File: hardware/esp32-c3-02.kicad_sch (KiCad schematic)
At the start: 15 parts, among them J3 GSD090012SEU, U3 ESP32-C3-WROOM-02-H4, U4 CP2102N-Axx-xQFN20, U5 USBLC6-2SC6, U6 W25Q32JVSSIQ

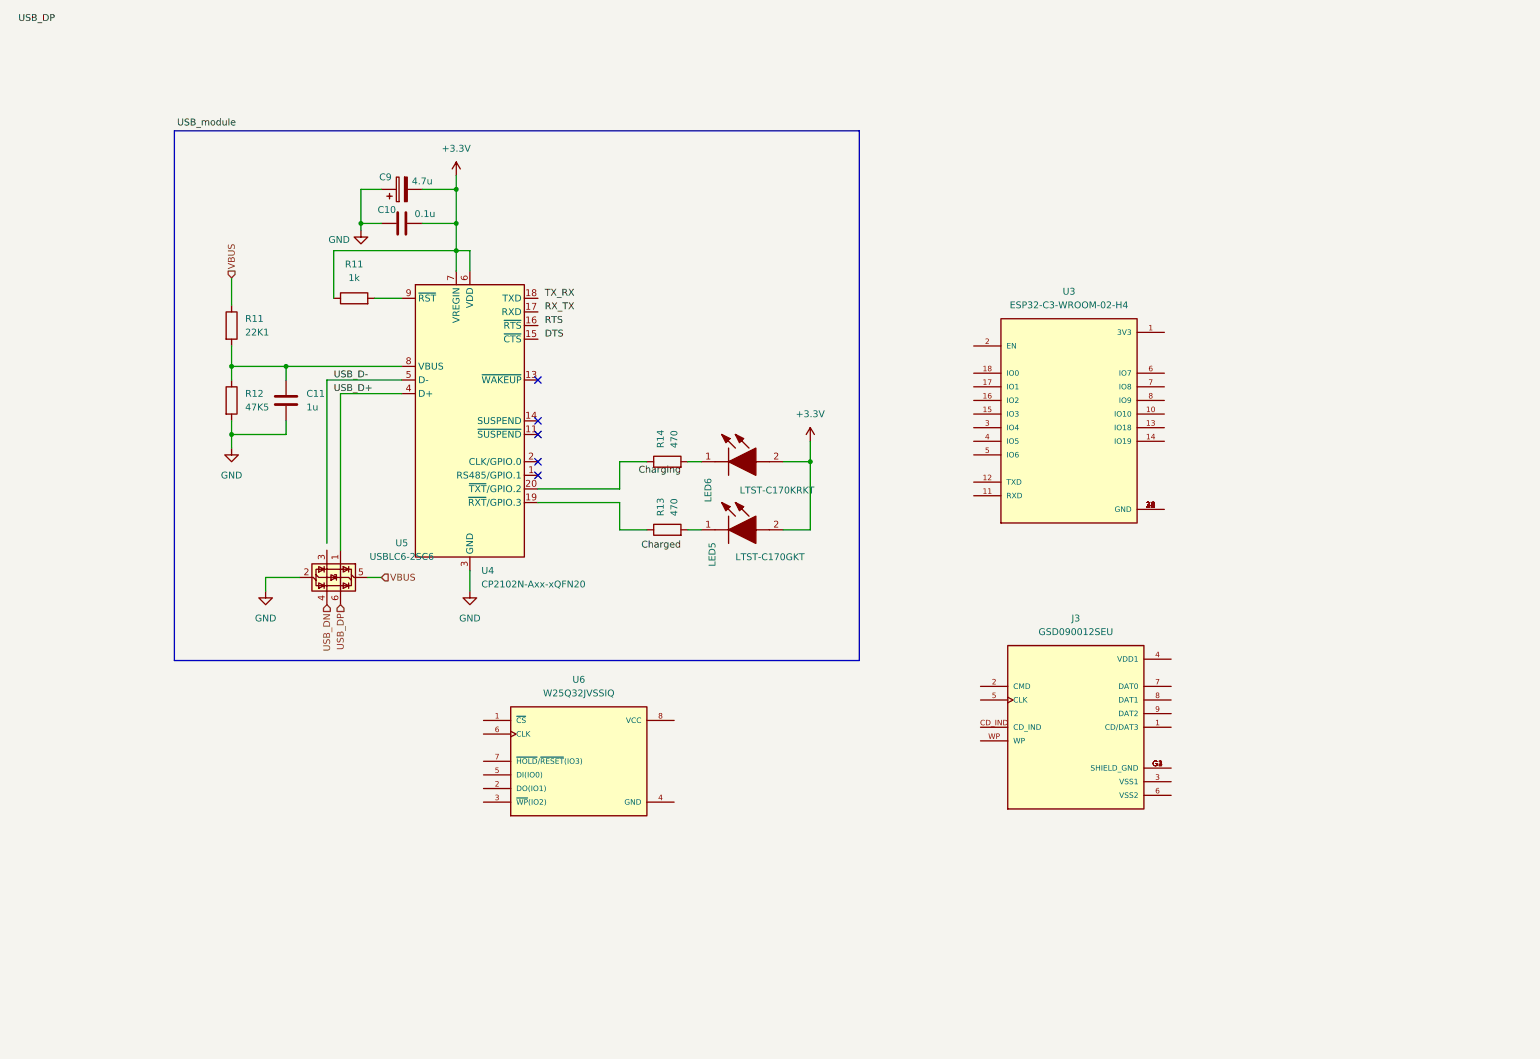
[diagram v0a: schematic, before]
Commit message: Completed the Esp32 schematics
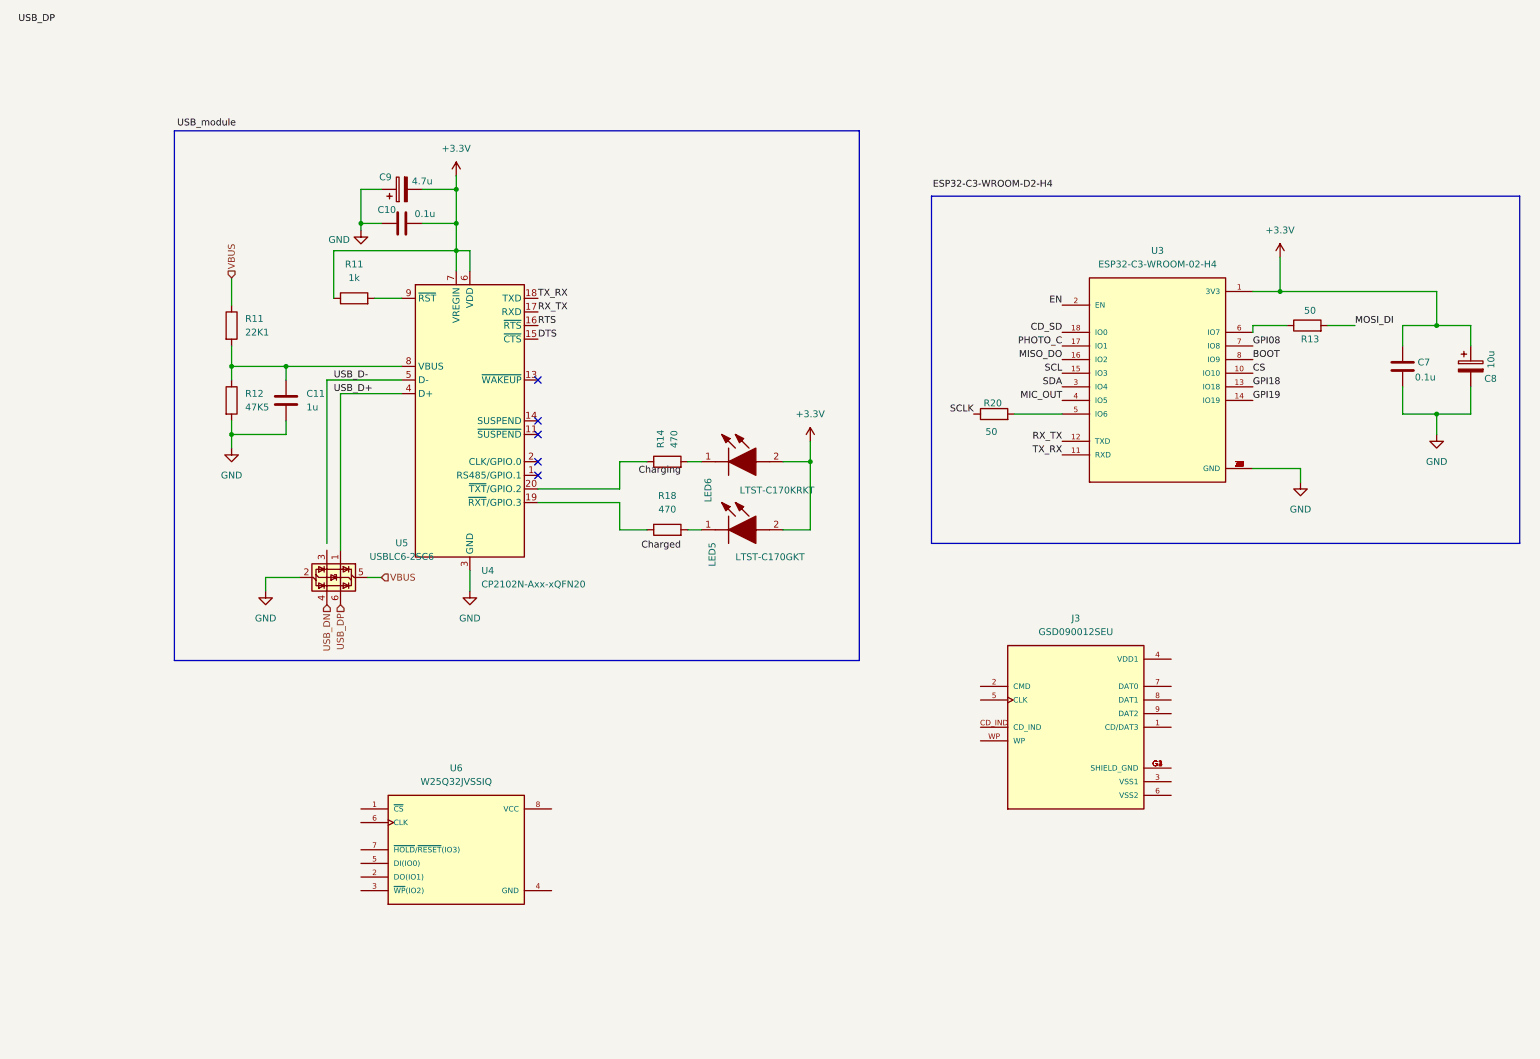
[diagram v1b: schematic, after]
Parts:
- added C7: 0.1u, symbol Device:C
- added C8: 10u, symbol Device:C_Polarized
- added R13, R20: 50, symbol Device:R
- renumbered R13 to R18
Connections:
- net +3.3V: now also U3.1 (3V3), C7.1, C8.1
- net DTS: now also U4.15 (~{CTS})
- net GND: now also U3.19 (GND), U3.20 (GND), U3.21 (GND), U3.22 (GND), U3.23 (GND), U3.24 (GND), U3.25 (GND), U3.26 (GND), U3.27 (GND), U3.28 (GND), U3.29 (GND), U3.30 (GND), U3.31 (GND), U3.32 (GND), U3.33 (GND), U3.34 (GND), U3.35 (GND), U3.36 (GND), U3.37 (GND), U3.38 (GND), U3.39 (GND), U3.9 (GND), C7.2, C8.2
- net RTS: now also U4.16 (~{RTS})
- net RX_TX: now also U3.12 (TXD), U4.17 (RXD)
- net TX_RX: now also U3.11 (RXD), U4.18 (TXD)
- net CS: now reaches U3.10 (IO10)
- net GPI18: now reaches U3.13 (IO18)
- net GPI19: now reaches U3.14 (IO19)
- net SCL: now reaches U3.15 (IO3)
- net MISO_DO: now reaches U3.16 (IO2)
- net PHOTO_C: now reaches U3.17 (IO1)
- net CD_SD: now reaches U3.18 (IO0)
- net EN: now reaches U3.2 (EN)
- net SDA: now reaches U3.3 (IO4)
- net MIC_OUT: now reaches U3.4 (IO5)
- net at U3.5 (IO6): now also R20.2
- net at U3.6 (IO7): now also R13.1
- net GPI08: now reaches U3.7 (IO8)
- net BOOT: now reaches U3.8 (IO9)
- new net MOSI_DI: R13.2
- new net SCLK: R20.1
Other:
- moved on the sheet: U3, U6

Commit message: Completed the SD card Module
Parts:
- added C12: 10u, symbol Device:C_Polarized
- added C13: 0.1u, symbol Device:C
- added R16: 50, symbol Device:R
- added R19: 10K, symbol Device:R
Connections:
- net CD_SD is gone; now on net CS_SD: U3.18 (IO0)
- net +3.3V: now also R19.1
- net GND: now also J3.3 (VSS1), J3.6 (VSS2), J3.8 (DAT1), J3.9 (DAT2), J3.G1 (SHIELD_GND), J3.G2 (SHIELD_GND), J3.G3 (SHIELD_GND), J3.G4 (SHIELD_GND), C12.2, C13.2
- net MISO_DO: now also R16.1
- net MOSI_DI: now also J3.2 (CMD)
- net SCLK: now also J3.5 (CLK)
- net CS_SD: now reaches J3.1 (CD/DAT3)
- net CS_SD: now also R19.2
- net at J3.4 (VDD1): now also C12.1, C13.1
- net at J3.7 (DAT0): now also R16.2
- no-connect marks 5 -> 7
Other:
- moved on the sheet: J3

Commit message: Added the Flash Memory
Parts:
- added C14: C, symbol Device:C
- added R22: 50, symbol Device:R
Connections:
- net +3.3V: now also C12.1, C13.1, J3.4 (VDD1), U6.3 (~{WP}(IO2)), U6.7 (~{HOLD}/~{RESET}(IO3)), U6.8 (VCC), C14.1
- net GND: now also U6.4 (GND), C14.2
- net MISO_DO: now also R22.1
- net MOSI_DI: now also U6.5 (DI(IO0))
- net at U6.2 (DO(IO1)): now also R22.2
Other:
- moved on the sheet: U6

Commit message: Added a Test Points to the Schematic
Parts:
- added TP1: Test MISO, symbol Connector:TestPoint
- added TP2: Test MOSI, symbol Connector:TestPoint
- added TP3: Test SCLK, symbol Connector:TestPoint
- added TP4: Test CS_SD, symbol Connector:TestPoint
- added TP5: Test_CS, symbol Connector:TestPoint
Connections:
- net CS: now also TP5.1
- net CS_SD: now also TP4.1
- net MISO_DO: now also TP1.1
- net MOSI_DI: now also TP2.1
- net SCLK: now also TP3.1
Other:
- added sheet Sensors (sensors.kicad_sch)
- added sheet User Interface (user_interface.kicad_sch)
- title: (none) -> Esp32, USB and Flash Memory
- moved on the sheet: C14, R22, U6

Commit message: Completed the Oled display and breakout for remaining pins
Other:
- sheet Sensors ports: added MIC_OUT, PHOTO_C, SCL, SDA; removed none
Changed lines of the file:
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@@
 		)
 	)
+	(label "MIC_OUT"
+		(at 154.94 140.97 0)
+		(effects
+			(font
+				(size 1.27 1.27)
+			)
+			(justify left bottom)
+		)
+	)
 	(label "GPI19"
 		(at 231.14 72.39 0)
@@
 		)
 	)
+	(label "SDA"
+		(at 154.94 143.51 0)
+		(effects
+			(font
+				(size 1.27 1.27)
+			)
+			(justify left bottom)
+		)
+	)
 	(label "SCLK"
 		(at 163.83 62.23 0)
@@
 		)
 	)
+	(label "PHOTO_C"
+		(at 154.94 148.59 0)
+		(effects
+			(font
+				(size 1.27 1.27)
+			)
+			(justify left bottom)
+		)
+	)
 	(label "MOSI_DI"
 		(at 250.19 58.42 0)
@@
 		)
 	)
+	(label "SCL"
+		(at 154.94 146.05 0)
+		(effects
+			(font
+				(size 1.27 1.27)
+			)
+			(justify left bottom)
+		)
+	)
 	(label "BOOT"
 		(at 231.14 64.77 0)
@@
 			)
 		)
+		(pin "MIC_OUT" input
+			(at 154.94 140.97 0)
+			(effects
+				(font
+					(size 1.27 1.27)
+				)
+				(justify right)
+			)
+		)
+		(pin "PHOTO_C" input
+			(at 154.94 143.51 0)
+			(effects
+				(font
+					(size 1.27 1.27)
+				)
+				(justify right)
+			)
+		)
+		(pin "SCL" input
+			(at 154.94 146.05 0)
+			(effects
+				(font
+					(size 1.27 1.27)
+				)
+				(justify right)
+			)
+		)
+		(pin "SDA" input
+			(at 154.94 148.59 0)
+			(effects
+				(font
+					(size 1.27 1.27)
+				)
+				(justify right)
+			)
+		)

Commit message: Completed the user interface
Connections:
- net GPI18 is gone; now on net GPI08: U3.13 (IO18)
- net GPI19 is gone; now on net GPI08: U3.14 (IO19)
- net DTS renamed DTR
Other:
- sheet User Interface ports: added BOOT, DTR, EN, GPIO18, GPIO19, GPIO8, RTS, SCL, SDA; removed none

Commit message: Completed Assigning footprints and correcting some mistakes
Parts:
- C10: renamed from C14; value C -> 0.1u; footprint (none) -> Capacitor_SMD:C_0805_2012Metric
- C11: renamed from C7; footprint (none) -> Capacitor_SMD:C_0805_2012Metric
- C12: renamed from C13; footprint (none) -> Capacitor_SMD:C_0805_2012Metric
- C7: renamed from C11; footprint (none) -> Capacitor_SMD:C_0805_2012Metric
- C9: renamed from C10; footprint (none) -> Capacitor_SMD:C_0805_2012Metric
- LED5: renamed from LED6; footprint LEDC2012X120N -> (none)
- LED6: renamed from LED5; footprint LEDC2012X120N -> (none)
- R11, R12, R19: footprint (none) -> Resistor_SMD:R_0805_2012Metric
- R13: renamed from R22; footprint (none) -> Resistor_SMD:R_0805_2012Metric
- R14: renamed from R11; footprint (none) -> Resistor_SMD:R_0805_2012Metric
- R15: renamed from R14; footprint (none) -> Resistor_SMD:R_0805_2012Metric
- R16: renamed from R18; footprint (none) -> Resistor_SMD:R_0805_2012Metric
- R17: renamed from R20; footprint (none) -> Resistor_SMD:R_0805_2012Metric
- R18: renamed from R16; footprint (none) -> Resistor_SMD:R_0805_2012Metric
- R20: renamed from R13; footprint (none) -> Resistor_SMD:R_0805_2012Metric
- TP1, TP2, TP3, TP4, TP5: footprint (none) -> TestPoint:TestPoint_Pad_D1.0mm
- renumbered C8 to C13, C12 to C14, C9 to C8, U5 to U2, U4 to U3, U6 to U4, U3 to U5
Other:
- note added: "ESP32-C3-WROOM-D2-H4"
- note added: "Flash Memory"
- note added: "SD card module"
- note added: "Test Points"
- note added: "USB_module"
